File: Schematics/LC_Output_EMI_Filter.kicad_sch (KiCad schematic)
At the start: 9 parts, among them J17 464379202, J3 23AH8786-Red, J4 23AH8785-Black

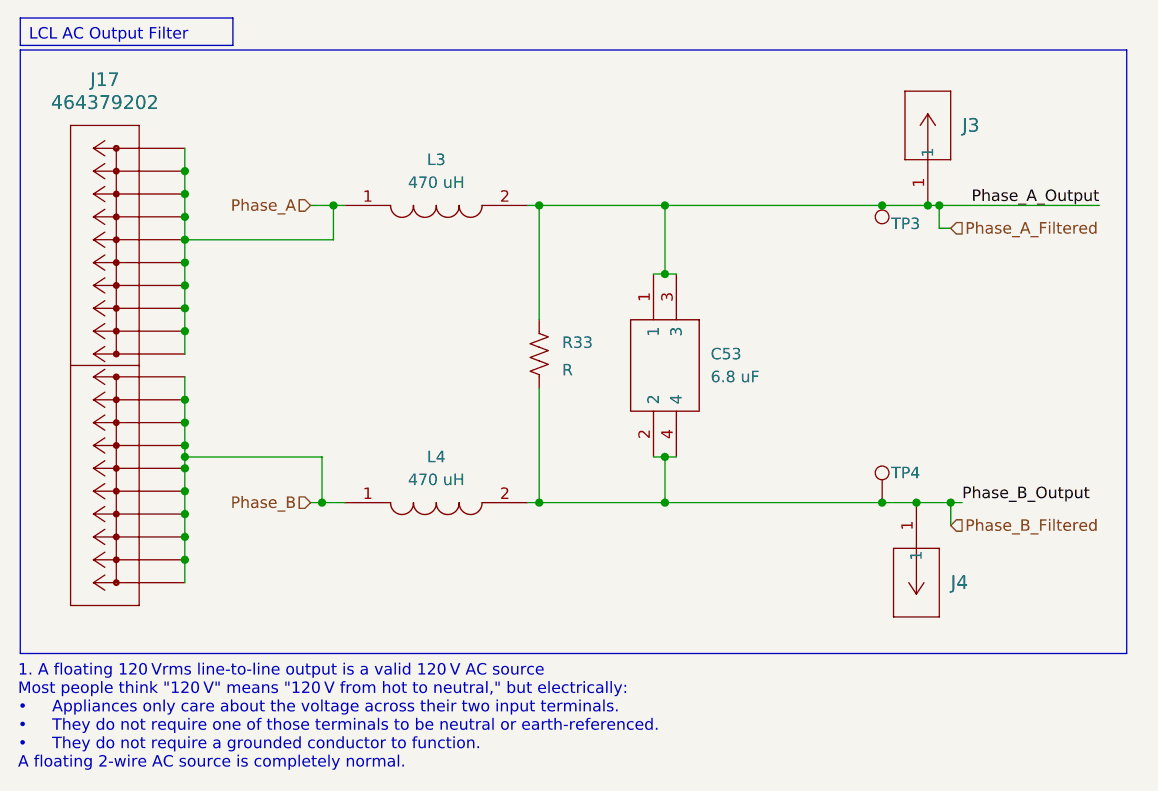
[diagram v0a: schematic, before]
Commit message: Adding Damping Resiter to AC Output Filter and mounting points
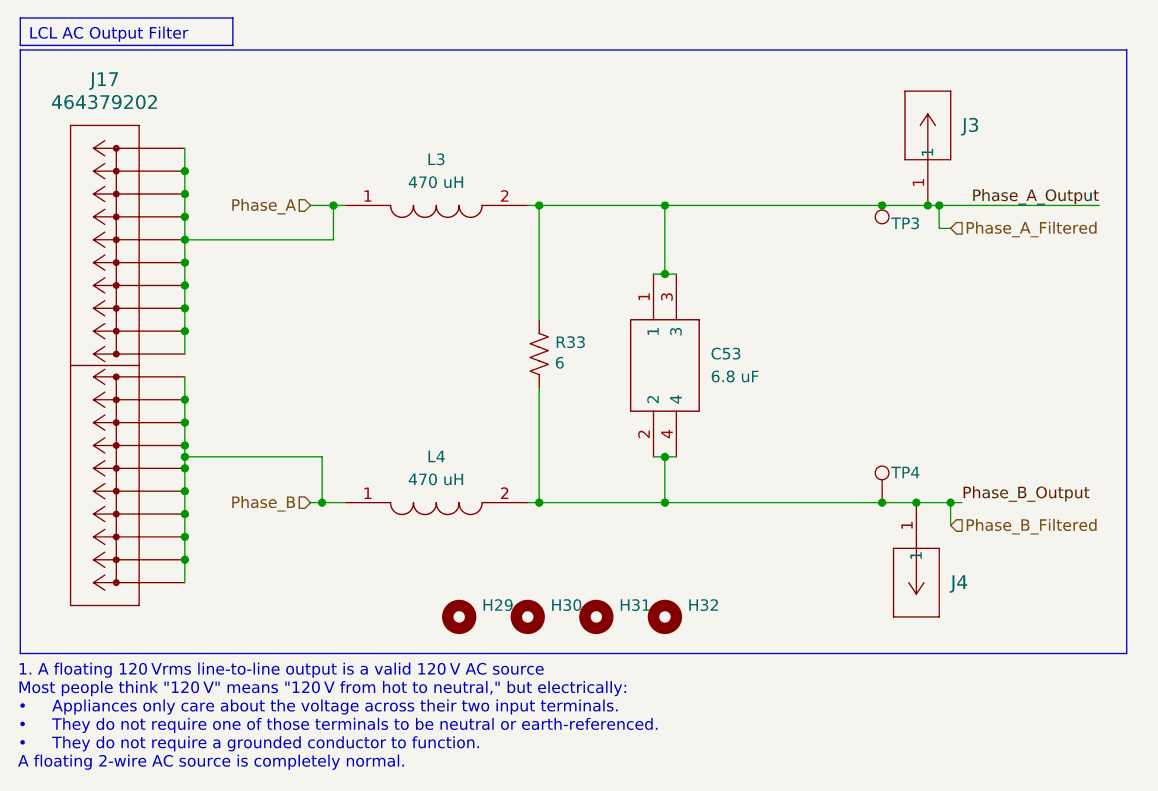
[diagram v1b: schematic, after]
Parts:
- added H29, H30, H31, H32: MountingHole, MountingHole:MountingHole_2.2mm_M2, symbol Mechanical:MountingHole
- R33: value R -> 6; symbol SiC_Inverter:3-2176794-3 -> SiC_Inverter:CW02B6R000JE12
